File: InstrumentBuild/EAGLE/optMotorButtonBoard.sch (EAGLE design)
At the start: 8 parts

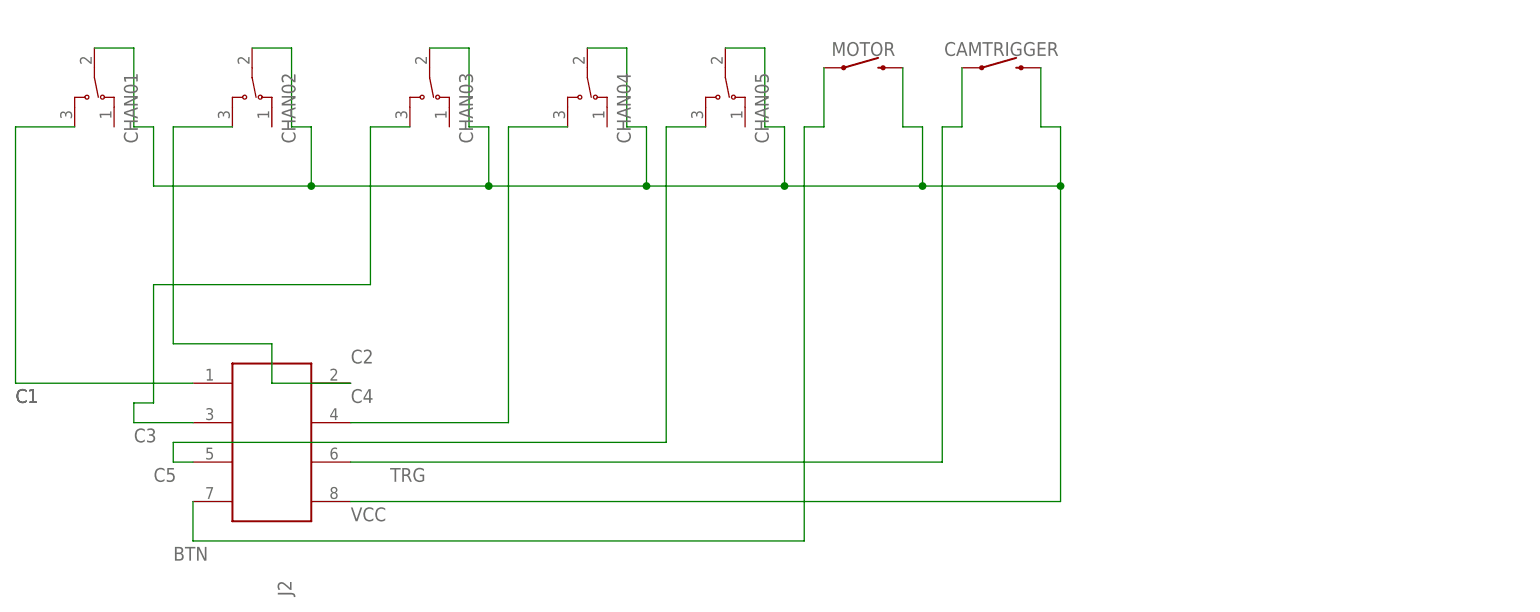
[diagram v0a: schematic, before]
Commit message: Updated top silk and added board's name to top.
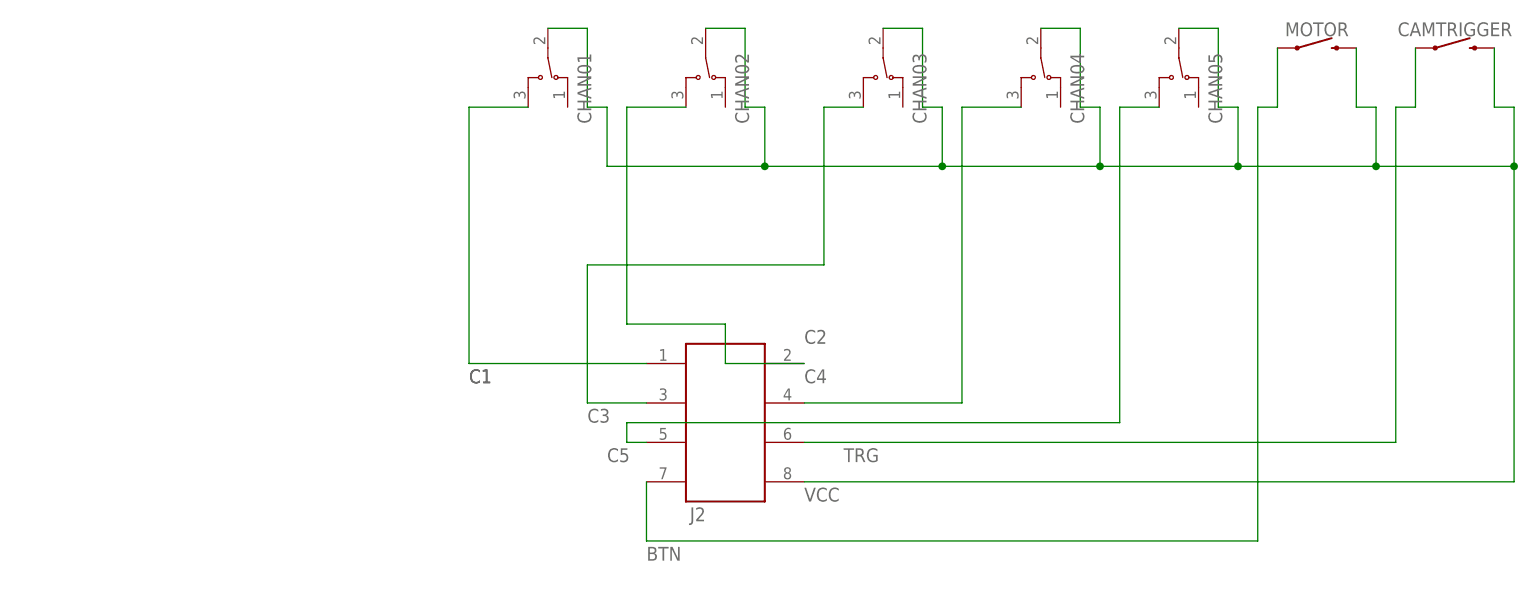
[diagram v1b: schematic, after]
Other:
- moved on the sheet: CAMTRIGGER, CHAN01, CHAN02, CHAN03, CHAN04, CHAN05, J2, MOTOR
